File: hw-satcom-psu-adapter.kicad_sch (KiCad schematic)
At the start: 84 parts, among them J1 XT60, J2 ATX-24, J3 Conn_02x02_Top_Bottom, J4 Conn_02x02_Top_Bottom, Q2 KIA3510AD, Q5 2N7002, Q6 2N7002, U1 Brick-DCDC, U10 ZXDN10, U2 LM5067, U3 EL3H7(B)(TA)-G, U4 EL3H7(B)(TA)-G, U5 AV10-48S05, U6 EL3H7(B)(TA)-G, U7 TPS3510, U8 ZXDN10, U9 ZXDN10

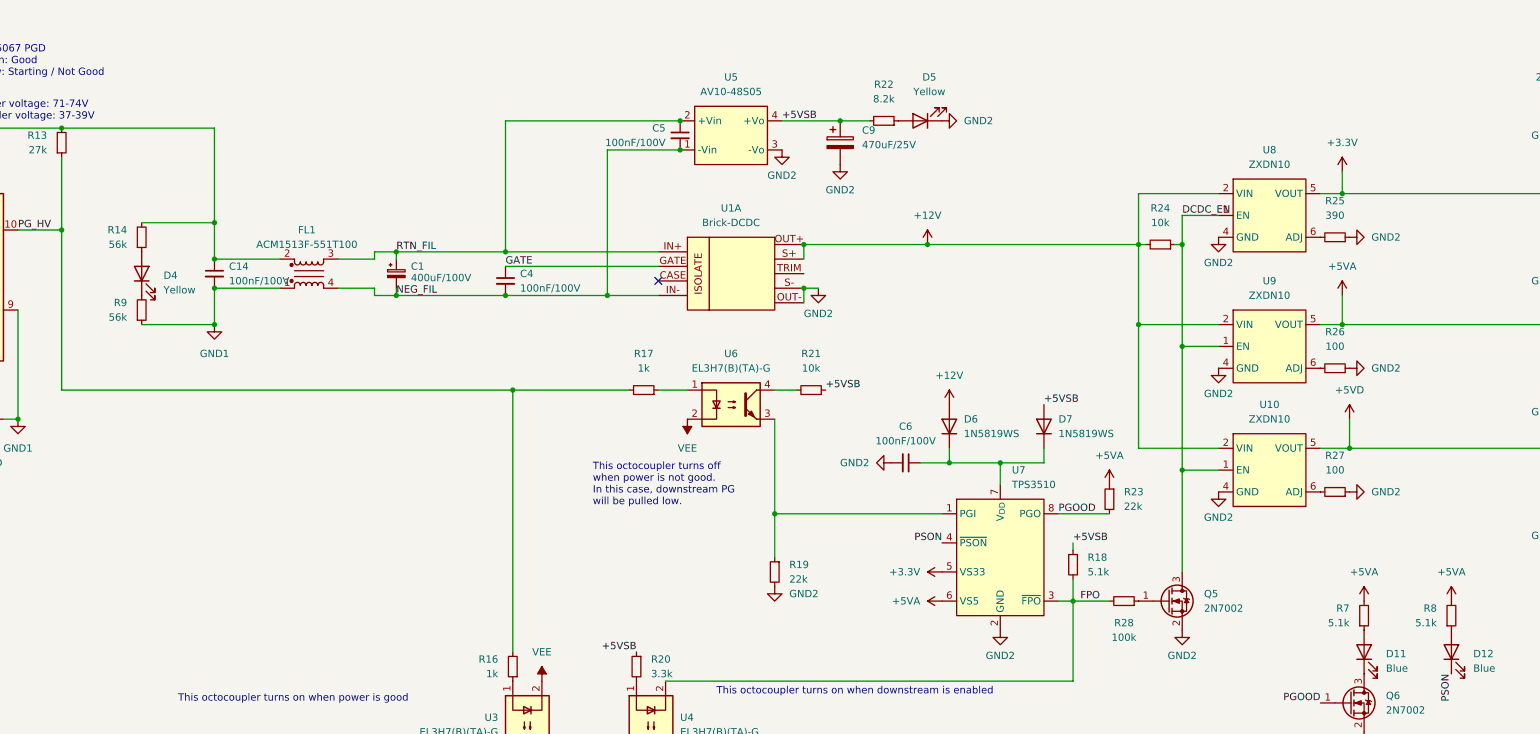
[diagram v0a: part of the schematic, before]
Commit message: Reduce LED brightness
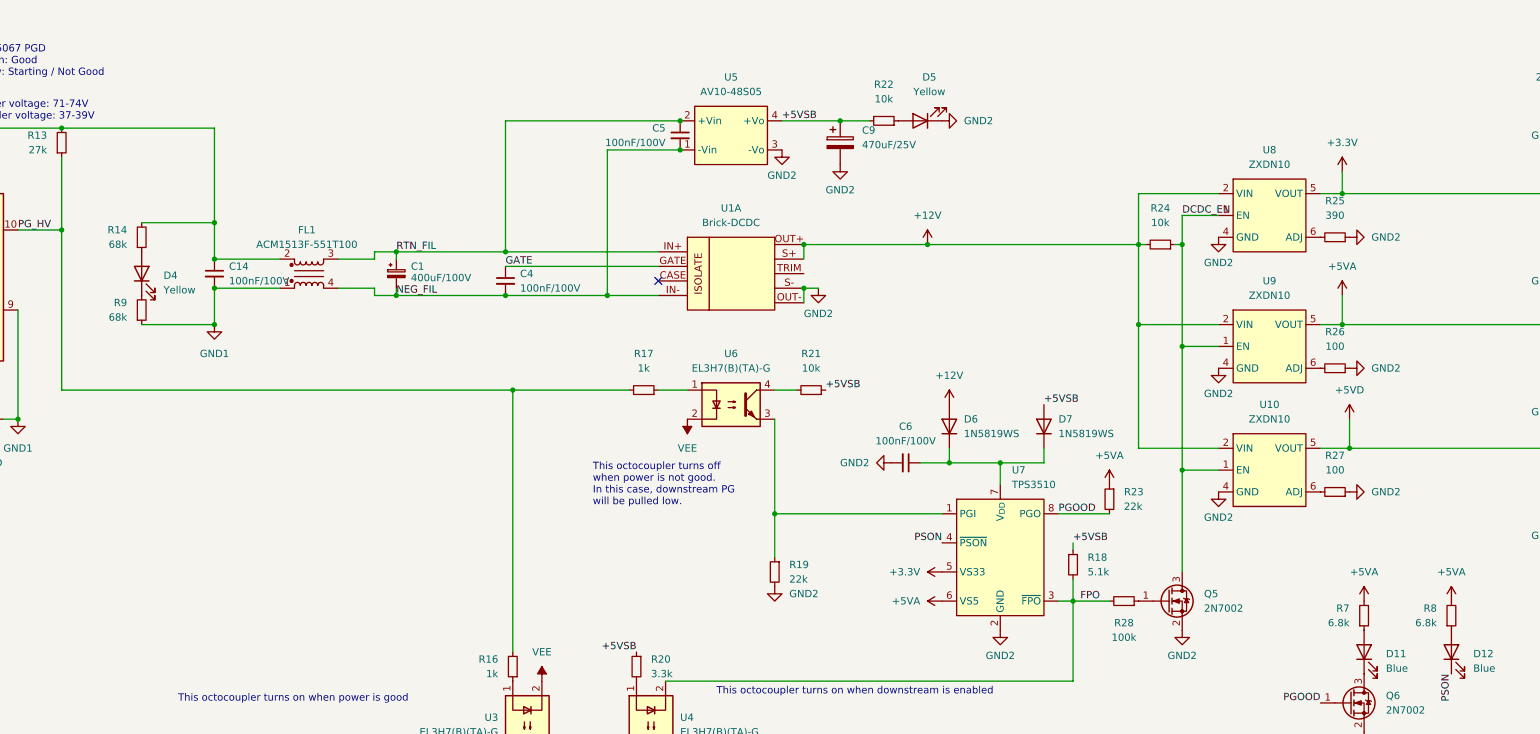
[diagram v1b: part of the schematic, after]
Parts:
- R14, R9: value 56k -> 68k
- R22: value 8.2k -> 10k
- R7, R8: value 5.1k -> 6.8k
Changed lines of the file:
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@@
       (effects (font (size 1.27 1.27)) (justify right))
     )
-    (property "Value" "56k" (id 1) (at 114.3 62.2299 0)
+    (property "Value" "68k" (id 1) (at 114.3 62.2299 0)
       (effects (font (size 1.27 1.27)) (justify right))
     )
@@
     (in_bom yes) (on_board yes) (fields_autoplaced)
     (property "Reference" "R22" (id 0) (at 246.38 34.29 90))
-    (property "Value" "8.2k" (id 1) (at 246.38 36.83 90))
+    (property "Value" "10k" (id 1) (at 246.38 36.83 90))
     (property "Footprint" "lc:0402_R" (id 2) (at 246.38 40.64 0)
       (effects (font (size 1.27 1.27)) hide)
@@
       (effects (font (size 1.27 1.27)) (justify right))
     )
-    (property "Value" "5.1k" (id 1) (at 327.66 128.2699 0)
+    (property "Value" "6.8k" (id 1) (at 327.66 128.2699 0)
       (effects (font (size 1.27 1.27)) (justify right))
     )
@@
       (effects (font (size 1.27 1.27)) (justify right))
     )
-    (property "Value" "5.1k" (id 1) (at 342.9 128.2699 0)
+    (property "Value" "6.8k" (id 1) (at 342.9 128.2699 0)
       (effects (font (size 1.27 1.27)) (justify right))
     )
@@
       (effects (font (size 1.27 1.27)) (justify right))
     )
-    (property "Value" "56k" (id 1) (at 114.3 74.9299 0)
+    (property "Value" "68k" (id 1) (at 114.3 74.9299 0)
       (effects (font (size 1.27 1.27)) (justify right))
     )
@@
     )
     (path "/a1c4c3c4-06ef-4ede-b7de-cc6300e826d6"
-      (reference "R7") (unit 1) (value "5.1k") (footprint "lc:0402_R")
+      (reference "R7") (unit 1) (value "6.8k") (footprint "lc:0402_R")
     )
     (path "/c2dd7cc6-218f-4b5d-b15a-07d7240e6f7d"
-      (reference "R8") (unit 1) (value "5.1k") (footprint "lc:0402_R")
+      (reference "R8") (unit 1) (value "6.8k") (footprint "lc:0402_R")
     )
     (path "/d8137245-8784-44f2-b28b-e400ba76b910"
-      (reference "R9") (unit 1) (value "56k") (footprint "lc:0603_R")
+      (reference "R9") (unit 1) (value "68k") (footprint "lc:0603_R")
     )
     (path "/ccfd5d01-b1a4-4222-8bde-9f7c4ecc3217"
@@
     )
     (path "/47f077bb-6199-49e4-b239-9640b6a93500"
-      (reference "R14") (unit 1) (value "56k") (footprint "lc:0603_R")
+      (reference "R14") (unit 1) (value "68k") (footprint "lc:0603_R")
     )
     (path "/4b62317b-efa3-4e5f-b4f1-a8333e206ac1"
@@
     )
     (path "/515f6649-bcc4-4cbc-91cc-3d502d2b01ee"
-      (reference "R22") (unit 1) (value "8.2k") (footprint "lc:0402_R")
+      (reference "R22") (unit 1) (value "10k") (footprint "lc:0402_R")
     )
     (path "/3c1cab6f-da6a-4fe3-aa97-ceada2e38d2b"
